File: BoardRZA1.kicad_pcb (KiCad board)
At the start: 4 copper layers, 99.9 x 80 mm, 189 parts, among them CON1 USB-MINI-B, CON2 USB-A-PCB, CON3 microSD, CON4 BARREL_JACK, J1 HR911105A, J2 SIL38, K1 CONN_3, P1 CONN_5X2, P10 CONN_1, P11 CONN_1, P12 CONN_1, P13 CONN_1, P14 CONN_1, P15 CONN_1, P16 CONN_1, P17 CONN_1, P2 CONN_1, P3 CONN_1, P4 CONN_1, P5 CONN_1, P6 CONN_1, P7 CONN_1, P8 CONN_1, P9 CONN_1, SW1 RESET, SW2 NMI, SW3 SW0, SW4 SW1, U1 RZ-A1L, U2 13MHz, U3 48MHz, U4 N25QXXX, U5 AS4C16M16S, U6 BA3259HFP, U7 BU42xx, U8 KSZ8041MLL, U9 25MHz, X1 32.768k

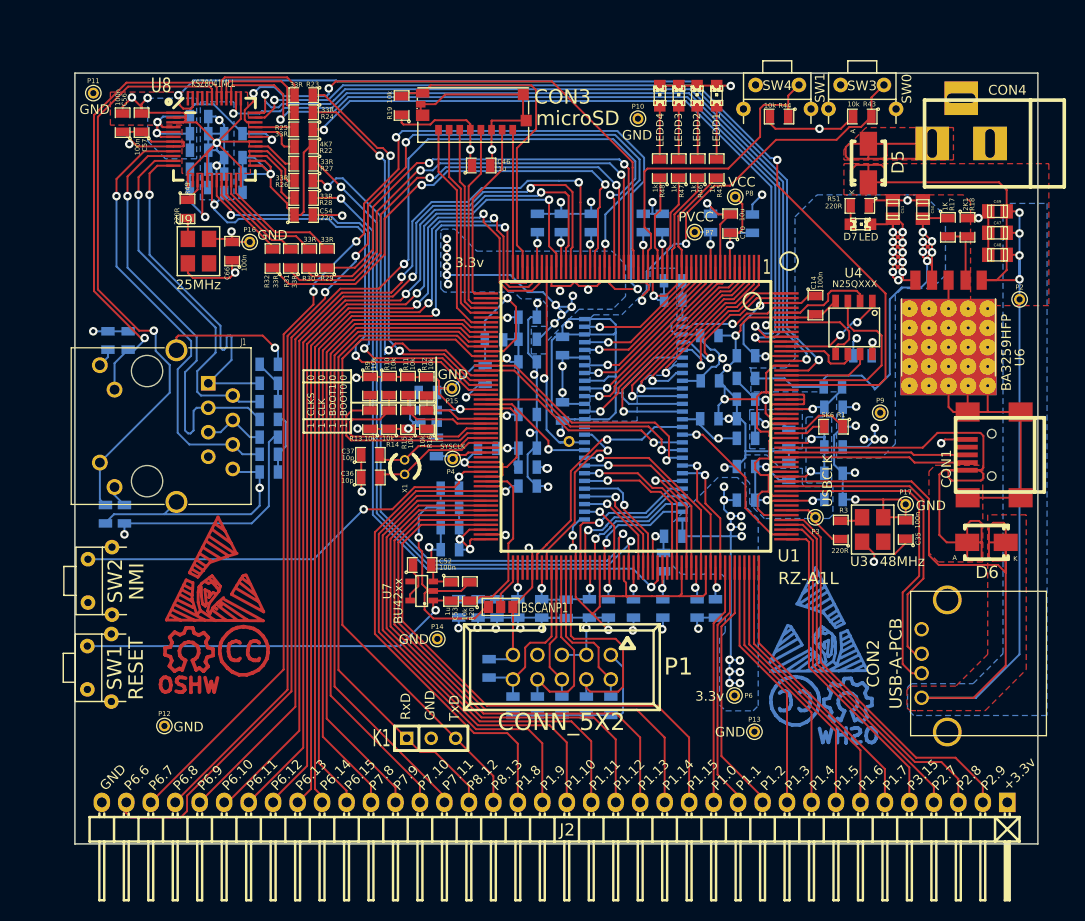
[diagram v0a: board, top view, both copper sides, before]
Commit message: Added VGA out, remove eth
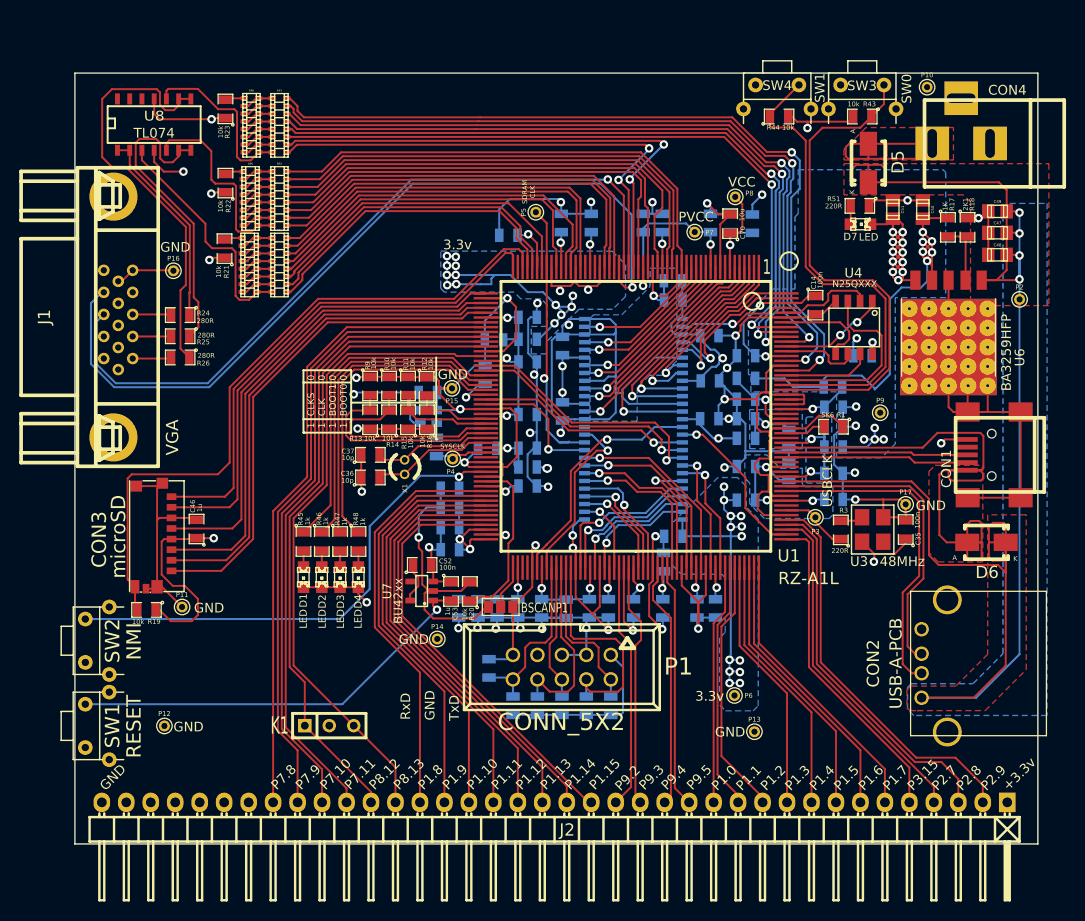
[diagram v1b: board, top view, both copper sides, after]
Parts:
- removed C54, C63: 22u, footprints:SM0805
- removed C55, C56, C57, C59, C60, C61, C62, C64, C65, C66: 100n, footprints:SM0805
- removed C58: 100p, footprints:SM0805
- removed L10: BLM18PG600, footprints:SM0805
- removed R27, R28, R29, R30, R31, R32: 33R, footprints:SM0805
- removed R33, R34, R35: 4K7, footprints:SM0805
- removed R36, R37, R49: 220R, footprints:SM0805
- removed R38, R39, R40, R41: 49.9, footprints:SM0805
- removed SYM (x2): Symbol_OSHW-Logo_CopperTop_07Jul2012, Symbols:Symbol_OSHW-Logo_CopperTop
- removed Sym (x2): Symbol_ESD-Logo_CopperTop_21Apr2011, Symbols:Symbol_ESD-Logo_CopperTop
- removed Sym (x2): Symbol_CreativeCommons_Typ2_CopperTop_Small, Symbols:Symbol_CreativeCommons_CopperTop_Type2_Small
- removed U9: 25MHz, footprints:OSC_4PIN
- added RP1: 20k, Resistors_SMD:r_cat16-8, F.Cu at (41.1, 37.5)
- added RP2: 20k, Resistors_SMD:r_cat16-8, F.Cu at (41.1, 30.6)
- added RP3: 20k, Resistors_SMD:r_cat16-8, F.Cu at (41.1, 23.0)
- added RP4: 10k, Resistors_SMD:r_cat16-8, F.Cu at (38.0, 37.5)
- added RP5: 10k, Resistors_SMD:r_cat16-8, F.Cu at (38.1, 30.6)
- added RP6: 10k, Resistors_SMD:r_cat16-8, F.Cu at (38.2, 23.0)
- J1: value HR911105A -> VGA; footprint footprints:RJ45_Pulse_J403-A -> footprints:DB_15F-VGA
- P5: moved to F.Cu
- R21: value 6.49k -> 10k; moved to F.Cu
- R22: value 4K7 -> 10k
- R23: value 33R -> 10k
- R24, R25, R26: value 33R -> 280R
- U8: value KSZ8041MLL -> TL074; footprint footprints:LQFP48-M05 -> SMD_Packages:SO14E
- moved D1 65.8 mm to (43.6, 69.9), turned to 270 degrees
- moved D2 63.4 mm to (45.5, 69.9), turned to 270 degrees
- moved D3 61.1 mm to (47.4, 69.9), turned to 270 degrees
- moved D4 58.9 mm to (49.3, 69.9), turned to 270 degrees
- moved R19 58.7 mm to (27.3, 73.3), turned to 180 degrees
- moved R45 57.8 mm to (43.6, 66.2), turned to 270 degrees
- moved R46 55.0 mm to (45.5, 66.2), turned to 270 degrees
- moved P11 54.1 mm to (31.0, 73.0)
- moved R47 52.3 mm to (47.4, 66.2), turned to 270 degrees
- moved CON3 50.7 mm to (31.2, 65.4), turned to 270 degrees
- moved R48 49.8 mm to (49.3, 66.2), turned to 270 degrees
- moved C46 47.9 mm to (32.5, 64.9), turned to 90 degrees
- moved P10 30.2 mm to (108.3, 19.1)
- moved R25 25.0 mm to (30.8, 44.9)
- moved R24 24.6 mm to (30.8, 42.7)
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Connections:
- CON1 pad 4: Net-(CON1-Pad4) -> (no net)
- J1 pad 10: /ET_LED0 -> VSS
- J1 pad 11: /ET_LED1 -> (no net)
- J1 pad 12: Net-(J1-Pad12) -> (no net)
- J1 pad 13: VSS -> /LCD_HSYNC
- J1 pad 14: VSS -> /LCD_VSYNC
- J1 pad 4: Net-(J1-Pad4) -> (no net)
- J1 pad 5: Net-(J1-Pad4) -> VSS
- J1 pad 6: Net-(J1-Pad6) -> VSS
- J1 pad 7: Net-(J1-Pad7) -> VSS
- J1 pad 9: Net-(J1-Pad9) -> VSS
- J2 pad 14: /P1_15 -> /P9_5
- J2 pad 15: /P1_14 -> /P9_4
- J2 pad 16: /P1_13 -> /P9_3
- J2 pad 17: /P1_12 -> /P9_2
- J2 pad 18: /P1_11 -> /P1_15
- J2 pad 19: /P1_10 -> /P1_14
- J2 pad 20: /P1_9 -> /P1_13
- J2 pad 21: /P1_8 -> /P1_12
- J2 pad 22: /P8_13 -> /P1_11
- J2 pad 23: /P8_12 -> /P1_10
- J2 pad 24: /P7_11 -> /P1_9
- J2 pad 25: /P7_10 -> /P1_8
- J2 pad 26: /P7_9 -> /P8_13
- J2 pad 27: /P7_8 -> /P8_12
- J2 pad 28: /P6_15 -> /P7_11
- J2 pad 29: /P6_14 -> /P7_10
- J2 pad 30: /P6_13 -> /P7_9
- J2 pad 31: /P6_12 -> /P7_8
- J2 pad 32: /P6_11 -> (no net)
- J2 pad 33: /P6_10 -> (no net)
- J2 pad 34: /P6_9 -> (no net)
- J2 pad 35: /P6_8 -> (no net)
- J2 pad 36: /P6_7 -> (no net)
- J2 pad 37: /P6_6 -> (no net)
- P1 pad 7: Net-(P1-Pad7) -> (no net)
- R21 pad 2: Net-(C58-Pad1) -> Net-(R21-Pad2)
- R22 pad 1: +3.3V -> VSS
- R23 pad 1: /ET_CRS -> VSS
- R24 pad 1: /ET_COL -> Net-(R24-Pad1)
- R24 pad 2: Net-(R24-Pad2) -> Net-(J1-Pad3)
- R25 pad 1: /ET_TXCLK -> Net-(R25-Pad1)
- R25 pad 2: Net-(R25-Pad2) -> Net-(J1-Pad2)
- R26 pad 1: /ET_RXCLK -> Net-(R26-Pad1)
- R26 pad 2: Net-(R26-Pad2) -> Net-(J1-Pad1)
- U1 pad 107: Net-(U1-Pad107) -> (no net)
- U1 pad 108: Net-(U1-Pad108) -> (no net)
- U1 pad 127: /ET_RXCLK -> /P9_2
- U1 pad 129: /ET_RXER -> /P9_3
- U1 pad 135: /ET_RXDV -> /P9_4
- U1 pad 137: Net-(U1-Pad137) -> /P9_5
- U1 pad 164: Net-(U1-Pad164) -> (no net)
- U1 pad 17: /LED0 -> /LCD_DATA8
- U1 pad 188: Net-(U1-Pad188) -> /SW0
- U1 pad 189: /PHY_RESET -> /SW1
- U1 pad 19: /LED1 -> /LCD_DATA9
- U1 pad 192: /ET_TXD0 -> /LCD_DATA0
- U1 pad 194: /ET_TXD1 -> /LCD_DATA1
- U1 pad 198: /ET_TXD2 -> /LCD_DATA2
- U1 pad 199: /ET_TXD3 -> /LCD_DATA3
- U1 pad 20: /LED2 -> /LCD_DATA10
- U1 pad 200: /ET_TXCLK -> /LCD_DATA4
- U1 pad 201: /TX_TXER -> /LCD_DATA5
- U1 pad 22: /LED3 -> /LCD_DATA11
- U1 pad 24: /SW1 -> /LCD_DATA12
- U1 pad 26: /SW0 -> /LCD_DATA13
- U1 pad 27: /ET_TXEN -> /LCD_DATA6
- U1 pad 28: /ET_RXD0 -> /LCD_DATA7
- U1 pad 29: /ET_RXD1 -> /LCD_HSYNC
- U1 pad 30: /ET_RXD2 -> /LCD_VSYNC
- U1 pad 31: /P6_6 -> /LCD_DATA14
- U1 pad 32: /P6_7 -> /LCD_DATA15
- U1 pad 33: /P6_8 -> /LCD_DATA16
- U1 pad 35: /ET_RXD3 -> (no net)
- U1 pad 37: /P8_11 -> (no net)
- U1 pad 38: /P6_9 -> /LCD_DATA17
- U1 pad 40: /P6_10 -> /LCD_DATA18
- U1 pad 41: /P6_11 -> /LCD_DATA19
- U1 pad 43: /P6_12 -> /LCD_DATA20
- U1 pad 46: /P6_13 -> /LCD_DATA21
- U1 pad 48: /P6_14 -> /LCD_DATA22
- U1 pad 49: /P6_15 -> /LCD_DATA23
- U1 pad 51: /SD_WP_1 -> (no net)
- U1 pad 70: /ET_COL -> /LED0
- U1 pad 71: /ET_CRS -> /LED1
- U1 pad 72: /ET_MDC -> /LED2
- U1 pad 73: /ET_MDIO -> /LED3
- U1 pad 87: Net-(U1-Pad87) -> (no net)
- U2 pad 1: Net-(U2-Pad1) -> (no net)
- U3 pad 1: Net-(U3-Pad1) -> (no net)
- U5 pad 40: Net-(U5-Pad40) -> (no net)
- U7 pad 4: Net-(U7-Pad4) -> (no net)
- U8 pad 1: VSS -> Net-(R24-Pad1)
- U8 pad 10: Net-(J1-Pad3) -> /VGA_R
- U8 pad 11: Net-(J1-Pad2) -> VSS
- U8 pad 12: Net-(J1-Pad1) -> (no net)
- U8 pad 13: VSS -> (no net)
- U8 pad 14: Net-(U8-Pad14) -> (no net)
- U8 pad 2: VSS -> Net-(R24-Pad1)
- U8 pad 3: VSS -> /VGA_B
- U8 pad 4: /ET_1v8 -> +3.3V
- U8 pad 5: /ET_1v8 -> /VGA_G
- U8 pad 6: /ET_1v8 -> Net-(R25-Pad1)
- U8 pad 7: +3.3V -> Net-(R25-Pad1)
- U8 pad 8: +3.3V -> Net-(R26-Pad1)
- U8 pad 9: Net-(J1-Pad6) -> Net-(R26-Pad1)
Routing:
- net /P6_7: track 126.3 -> 0.00 mm, vias 4 -> 0
- net /P6_6: track 125.6 -> 0.00 mm, vias 2 -> 0
- net /P6_8: track 116.7 -> 0.00 mm, vias 4 -> 0
- net /PHY_RESET: track 107.7 -> 0.00 mm, vias 2 -> 0
- net /P6_9: track 100.4 -> 0.00 mm, vias 2 -> 0
- net /P6_10: track 97.6 -> 0.00 mm, vias 2 -> 0
- net /P6_11: track 95.2 -> 0.00 mm, vias 2 -> 0
- net /P6_12: track 91.3 -> 0.00 mm, vias 2 -> 0
- net /P6_13: track 90.0 -> 0.00 mm, vias 2 -> 0
- net /P6_14: track 88.0 -> 0.00 mm, vias 2 -> 0
- net /P6_15: track 87.3 -> 0.00 mm, vias 2 -> 0
- net /ET_TXD3: track 87.2 -> 0.00 mm, vias 2 -> 0
- net /LCD_VSYNC: track 0.00 -> 86.1 mm, vias 0 -> 1
- net /ET_TXD0: track 85.0 -> 0.00 mm, vias 2 -> 0
- net /ET_TXD2: track 84.7 -> 0.00 mm, vias 2 -> 0
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- removed copper zone on B.Cu, net /ET_1v8
- removed copper zone on F.Cu, net VSS
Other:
- board text added: "P9.2"
- board text added: "P9.3"
- board text added: "P9.4"
- board text added: "P9.5"
- board text removed: "P6.10"
- board text removed: "P6.11"
- board text removed: "P6.12"
- board text removed: "P6.13"
- board text removed: "P6.14"
- board text removed: "P6.15"
- board text removed: "P6.6"
- board text removed: "P6.7"
- board text removed: "P6.8"
- board text removed: "P6.9"

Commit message: Resize board, move VGA connector and R2R DAC
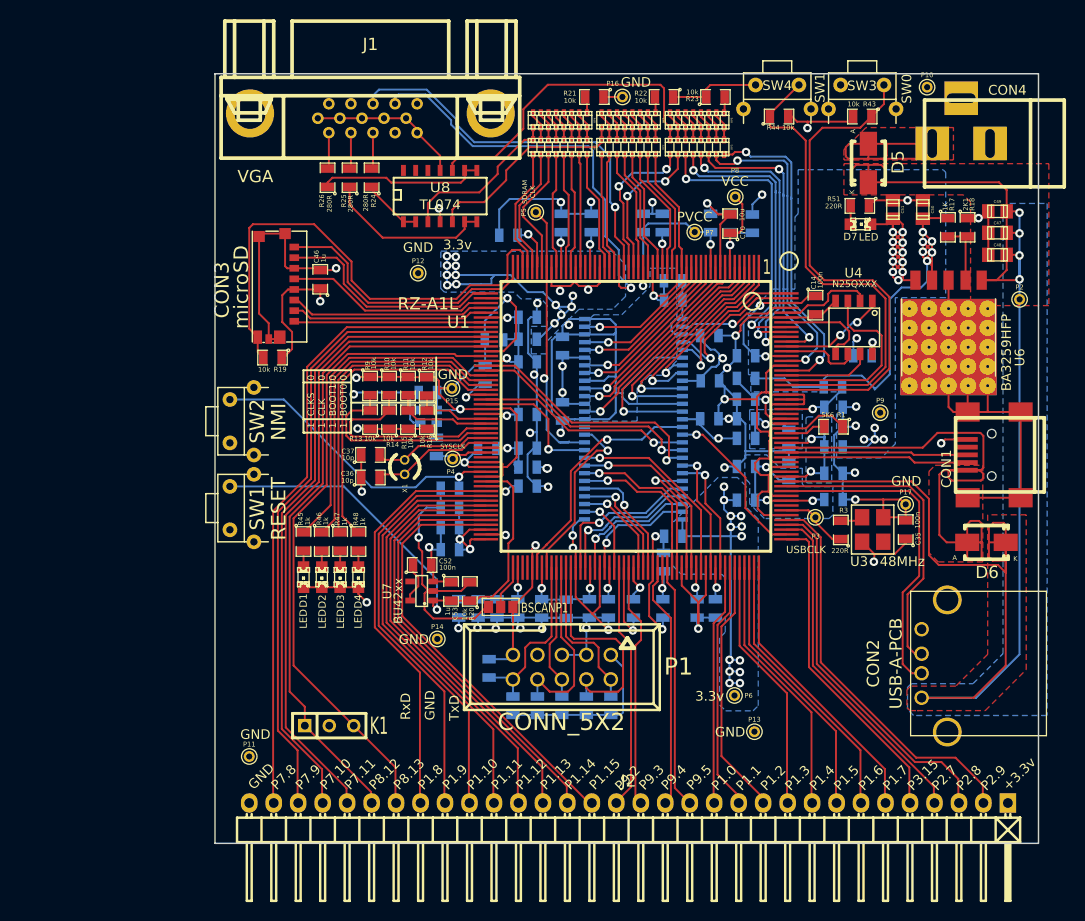
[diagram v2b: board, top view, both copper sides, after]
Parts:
- J2: value SIL38 -> SUPP32; footprint footprints:Pin_Header_Angled_1x38 -> Pin_Headers:Pin_Header_Angled_1x32
- moved P12 53.9 mm to (55.5, 38.4)
- moved R23 50.9 mm to (86.4, 20.1), turned to 0 degrees
- moved P16 50.0 mm to (76.7, 20.1)
- moved R22 46.4 mm to (81.0, 20.1), turned to 180 degrees
- moved RP6 46.3 mm to (84.5, 22.5), turned to 270 degrees
- moved RP3 43.4 mm to (84.5, 25.3), turned to 270 degrees
- moved R21 41.5 mm to (73.8, 20.1), turned to 180 degrees
- moved RP5 40.1 mm to (77.3, 22.5), turned to 270 degrees
- moved J1 37.5 mm to (50.5, 19.3), turned to 180 degrees
- moved RP2 36.6 mm to (77.3, 25.3), turned to 270 degrees
- moved RP4 35.6 mm to (70.2, 22.5), turned to 270 degrees
- moved RP1 31.6 mm to (70.2, 25.3), turned to 270 degrees
- moved U8 30.6 mm to (57.8, 30.2)
- moved R19 29.3 mm to (40.4, 47.1)
- moved C46 28.9 mm to (45.3, 39.0)
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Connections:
- J2 pad 32: (no net) -> VSS
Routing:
- net /LCD_DATA0: track 82.8 -> 33.7 mm
- net /LCD_DATA1: track 79.9 -> 32.6 mm
- net /LCD_DATA2: track 75.8 -> 29.8 mm
- net /LCD_DATA3: track 74.2 -> 29.6 mm
- net /LCD_VSYNC: track 86.1 -> 43.1 mm
- net /LCD_DATA4: track 73.2 -> 30.5 mm
- net /LCD_DATA5: track 71.5 -> 30.9 mm
- net /LCD_DATA8: track 51.2 -> 12.8 mm
- net /LCD_DATA6: track 53.8 -> 15.5 mm
- net /LCD_DATA9: track 50.6 -> 13.0 mm
- net /LCD_HSYNC: track 78.0 -> 40.9 mm
- net /LCD_DATA11: track 49.9 -> 12.8 mm
- net /LCD_DATA10: track 50.1 -> 13.1 mm
- net /LCD_DATA7: track 52.4 -> 16.2 mm
- net /LCD_DATA12: track 48.4 -> 12.7 mm
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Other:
- board size 99.9 x 80 mm -> 85.5 x 79.9 mm

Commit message: Some minor routing changes to probe new kicad assisted route
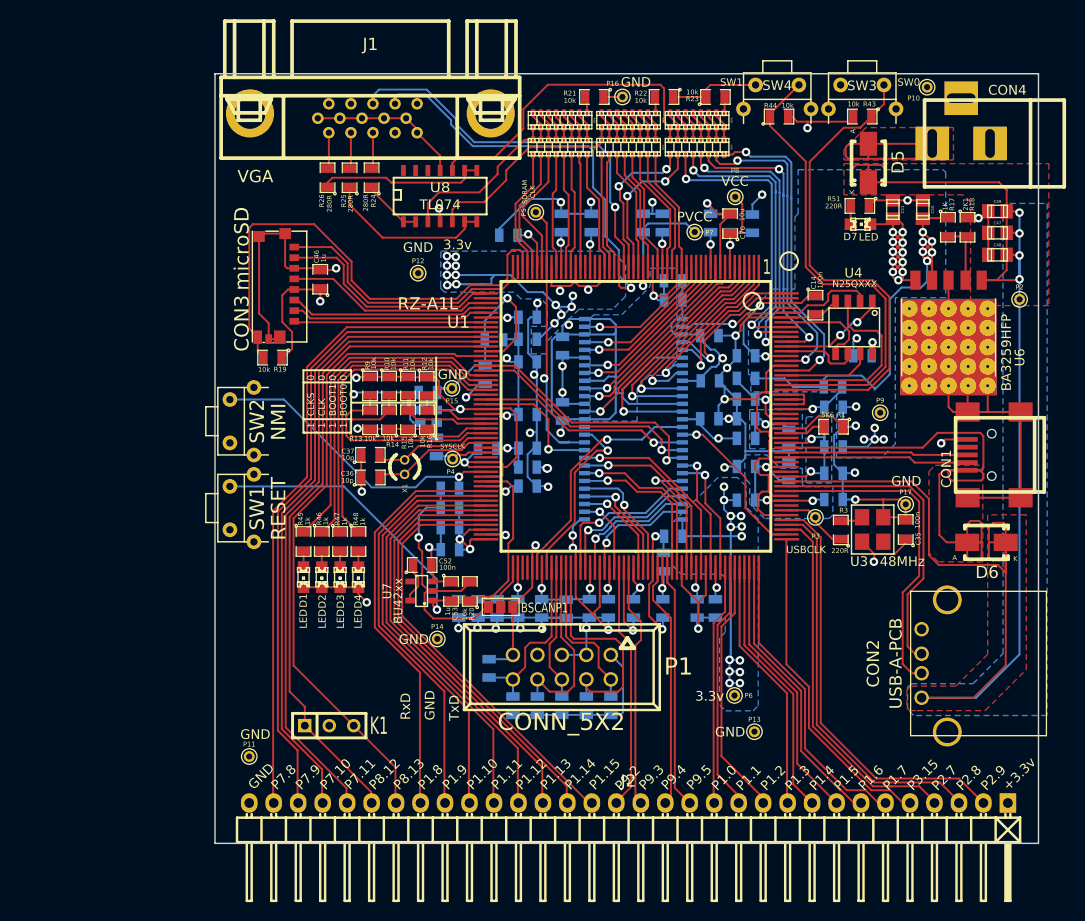
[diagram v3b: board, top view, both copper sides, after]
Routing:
- net /P2_7: track 35.6 -> 39.3 mm
- net /P2_9: track 41.2 -> 43.8 mm
- net /P2_8: track 38.8 -> 41.3 mm
- net /P1_7: track 29.8 -> 31.4 mm
- net /SW0: track 52.9 -> 51.6 mm
- net /SW1: track 52.0 -> 50.8 mm
- net VSS: track 572.6 -> 571.4 mm

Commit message: Update diagrams and pictures (1)
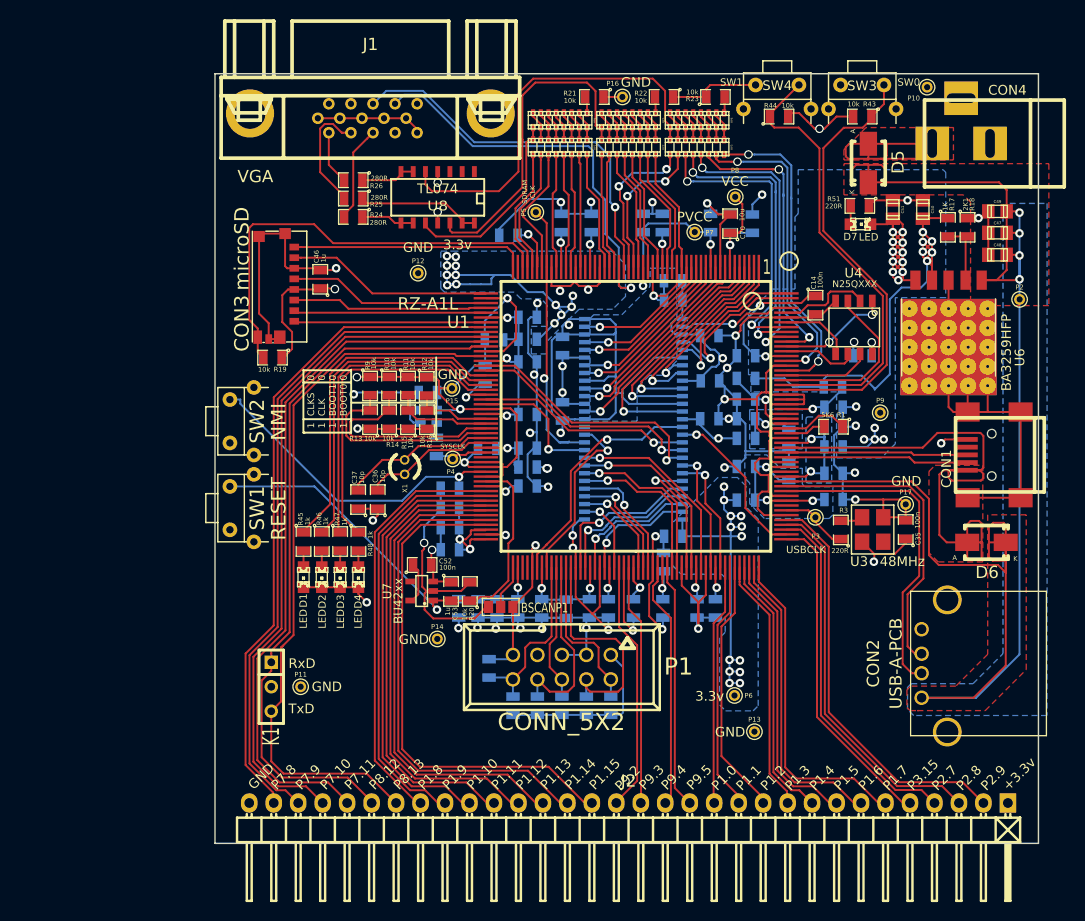
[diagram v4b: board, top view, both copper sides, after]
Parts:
- moved P11 8.99 mm to (43.3, 81.3)
- moved K1 7.25 mm to (40.3, 81.3), turned to 270 degrees
- moved C37 4.81 mm to (49.3, 61.8), turned to 90 degrees
- moved R24 4.49 mm to (48.8, 32.5), turned to 180 degrees
- moved R26 2.68 mm to (48.8, 28.7), turned to 180 degrees
- moved C36 2.41 mm to (51.3, 61.8), turned to 90 degrees
- moved R25 2.19 mm to (48.8, 30.6), turned to 180 degrees
- moved U8 0.46 mm to (57.5, 30.6), turned to 180 degrees
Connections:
- U8 pad 1: Net-(R24-Pad1) -> (no net)
- U8 pad 10: /VGA_R -> /VGA_B
- U8 pad 12: (no net) -> /VGA_G
- U8 pad 13: (no net) -> Net-(R25-Pad1)
- U8 pad 14: (no net) -> Net-(R25-Pad1)
- U8 pad 2: Net-(R24-Pad1) -> (no net)
- U8 pad 3: /VGA_B -> (no net)
- U8 pad 5: /VGA_G -> /VGA_R
- U8 pad 6: Net-(R25-Pad1) -> Net-(R26-Pad1)
- U8 pad 7: Net-(R25-Pad1) -> Net-(R26-Pad1)
- U8 pad 8: Net-(R26-Pad1) -> Net-(R24-Pad1)
- U8 pad 9: Net-(R26-Pad1) -> Net-(R24-Pad1)
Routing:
- net /VGA_G: track 21.8 -> 34.5 mm
- net Net-(R26-Pad1): track 17.4 -> 5.82 mm
- net /VGA_R: track 33.0 -> 41.9 mm
- net /PVCC: track 135.7 -> 144.4 mm
- net Net-(J1-Pad2): track 3.78 -> 12.1 mm
- net /P1_15: track 44.6 -> 52.7 mm
- net /P8_13: track 67.7 -> 75.1 mm
- net /P1_14: track 44.3 -> 51.4 mm
- net /SD_CD_1: track 52.1 -> 45.3 mm
- net /P8_12: track 67.5 -> 74.2 mm
- net Net-(J1-Pad3): track 3.78 -> 9.98 mm
- net /P1_13: track 44.1 -> 50.1 mm
- net /P7_11: track 67.4 -> 73.0 mm
- net VSS: track 571.4 -> 566.0 mm, vias 48 -> 49
- net /P1_12: track 44.0 -> 48.8 mm
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
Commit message: Actualized schematic
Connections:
- net Net-(P4-Pad1) renamed /SYS_CLK
